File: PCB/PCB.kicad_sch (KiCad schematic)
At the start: 1 part, among them U1 ESP32-S3-WROOM-1-N16R2

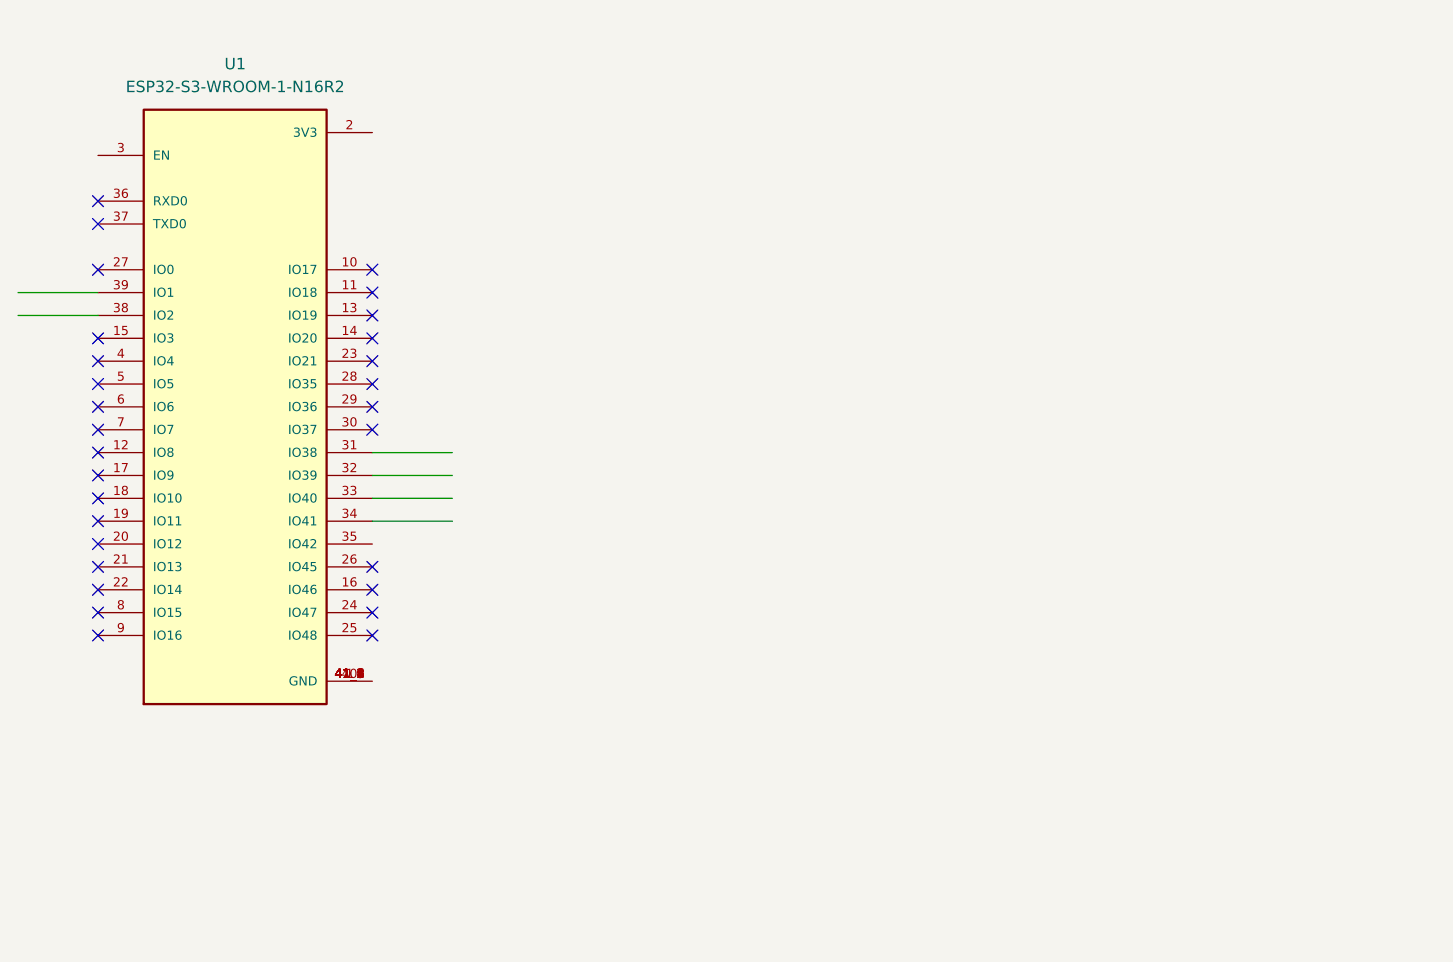
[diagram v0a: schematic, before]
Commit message: ESP32-S3 Schematic Section Added
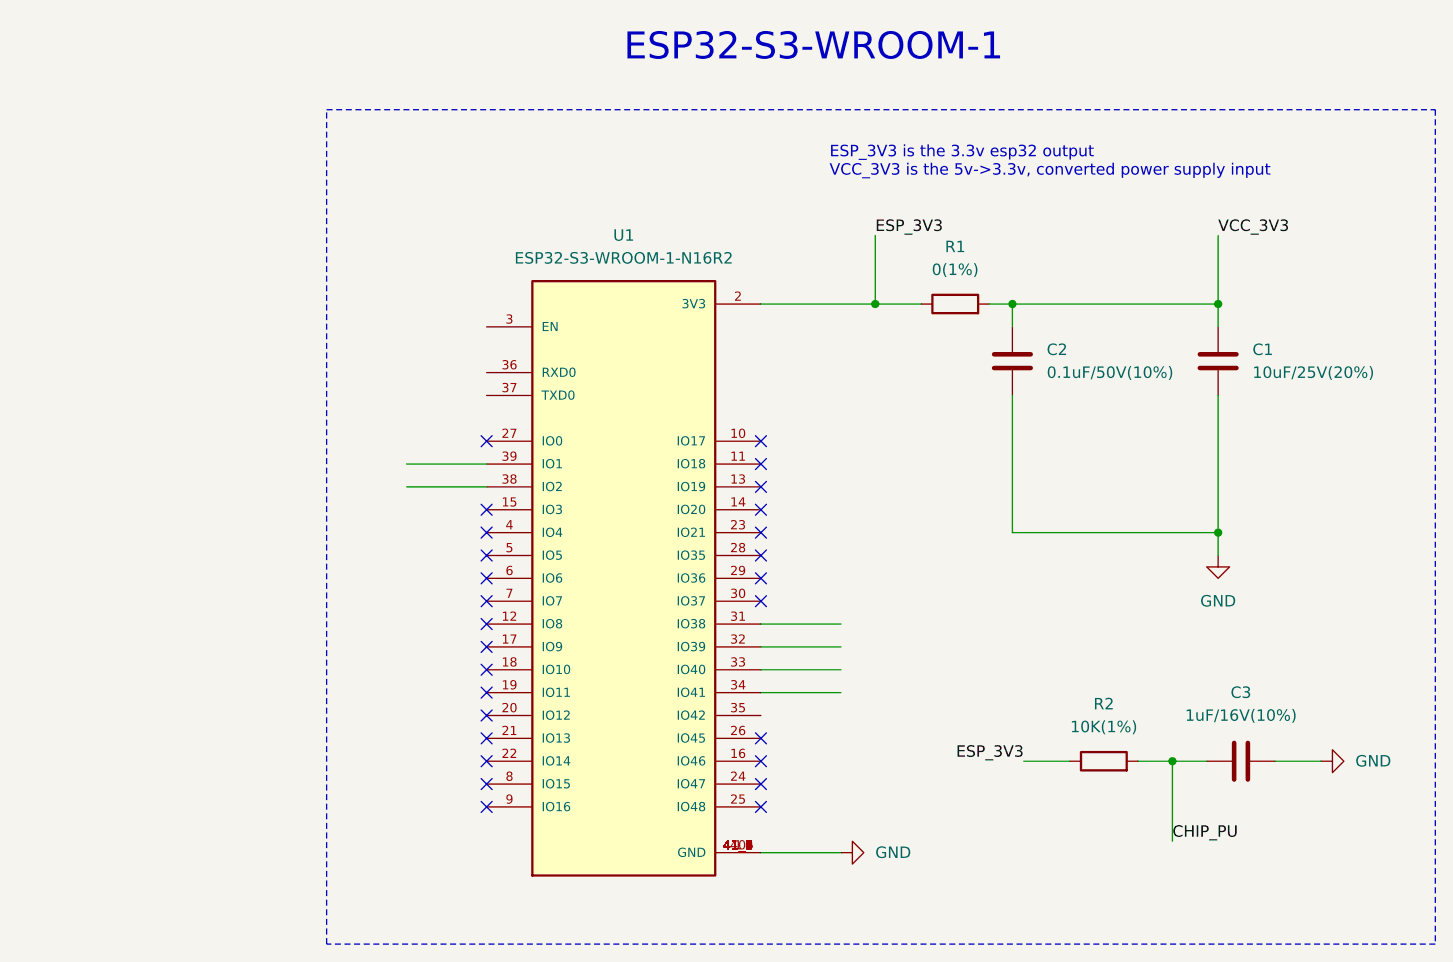
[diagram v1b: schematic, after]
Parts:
- added C1: 10uF/25V(20%), symbol Device:C
- added C2: 0.1uF/50V(10%), symbol Device:C
- added C3: 1uF/16V(10%), symbol Device:C
- added R1: 0(1%), symbol Device:R
- added R2: 10K(1%), symbol Device:R
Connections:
- net GND: now reaches U1.1 (GND), U1.40 (GND), U1.41_1 (GND), U1.41_2 (GND), U1.41_3 (GND), U1.41_4 (GND), U1.41_5 (GND), U1.41_6 (GND), U1.41_7 (GND), U1.41_8 (GND), U1.41_9 (GND)
- net GND: now also C1.2, C2.2, C3.2
- net ESP_3V3: now reaches U1.2 (3V3)
- net ESP_3V3: now also R1.1, R2.1
- new net CHIP_PU: C3.1, R2.2
- new net VCC_3V3: C1.1, C2.1, R1.2
- no-connect marks 29 -> 27
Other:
- note added: "ESP32-S3-WROOM-1"
- note added: "ESP_3V3 is the 3.3v esp32 output VCC_3V3 is the 5v->3.3v, converted power supply input"
- moved on the sheet: U1
